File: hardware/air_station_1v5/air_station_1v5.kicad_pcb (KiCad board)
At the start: 2 copper layers, 26.8 x 47.9 mm, 40 parts, among them J1 GCT-SIM7200-XRevA, J2 Micro_SD_Card, J4 BAT_PORT, J5 PROG_PORT, U1 A9G, U3 MCP73831-2-OT, U5 BMP388, U7 AP7312-1833, U9 MIC5225-3.3, X1 ENS160

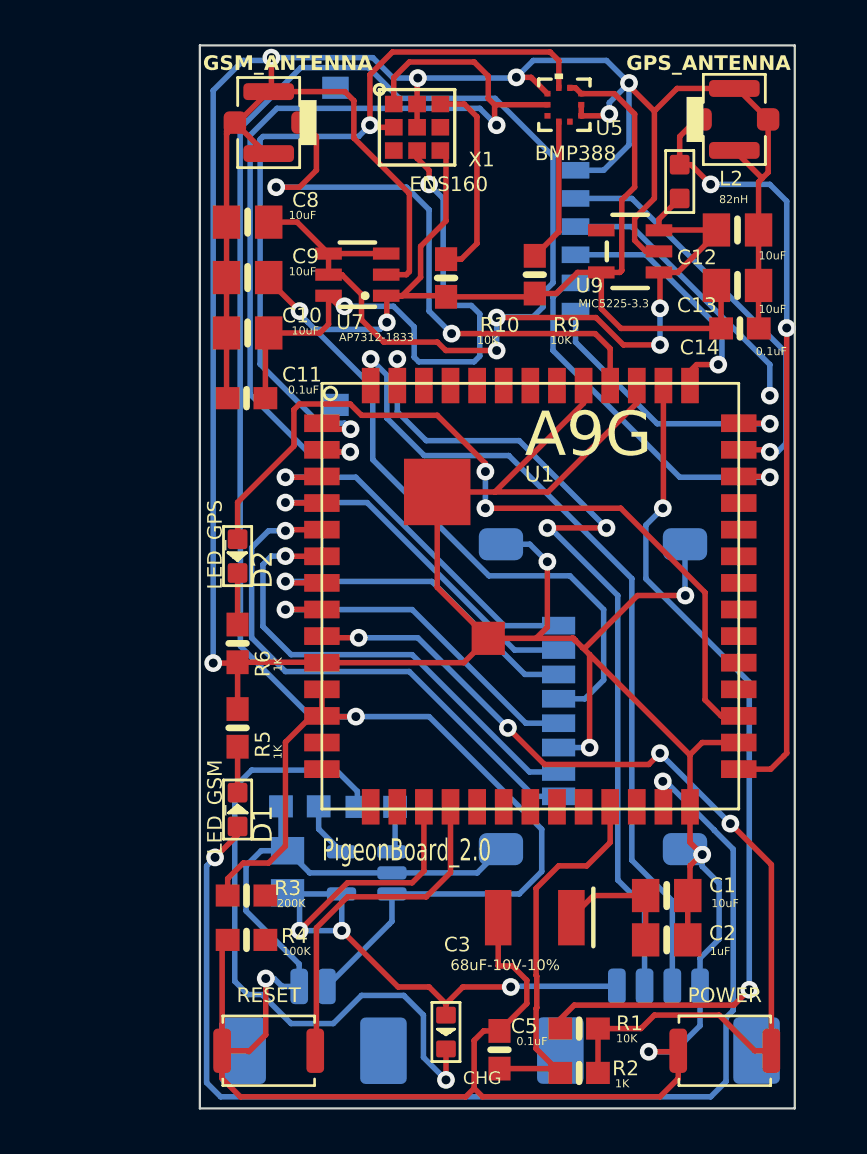
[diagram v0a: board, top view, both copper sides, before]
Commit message: update 1.9
I2C pullups update
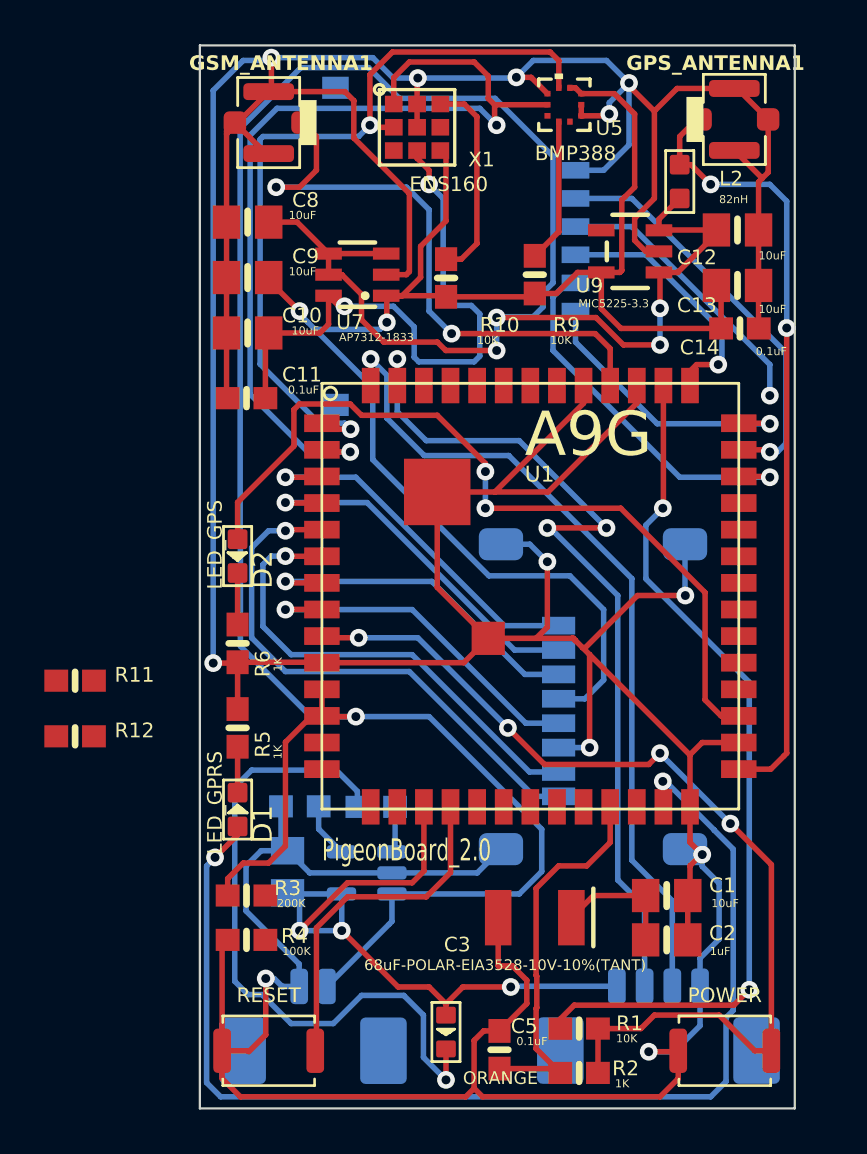
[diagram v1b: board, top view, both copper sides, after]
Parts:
- added R11: 4.7K, Adafruit BMP388:0603-NO, F.Cu at (70.3, 81.3)
- added R12: 4.7K, Adafruit BMP388:0603-NO, F.Cu at (70.3, 83.8)
- C3: value 68uF-10V-10% -> 68uF-POLAR-EIA3528-10V-10%(TANT)
- CHG1: renamed from CHG; value CHG -> ORANGE
- D1: value LED_GSM -> LED_GPRS
- J1: value GCT-SIM7200-XRevA -> SIM7200-6-0-18-00-X_REVA
- renumbered GPS_ANTENNA to GPS_ANTENNA1, GSM_ANTENNA to GSM_ANTENNA1
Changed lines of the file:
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@@
     (property "Sheetfile" "air_station_1v5.kicad_sch")
     (property "Sheetname" "")
-    (fp_text reference "GPS_ANTENNA" (at -4.877 -2.152 180) (layer "F.SilkS")
+    (fp_text reference "GPS_ANTENNA1" (at -4.877 -2.152 180) (layer "F.SilkS")
         (effects (font (size 0.66 0.66) (thickness 0.15) bold) (justify left bottom))
     )
@@
   )
   (footprint "Adafruit BMP388:0603-NO" (layer "F.Cu")
+    (at 70.27 83.82)
+    (property "Sheetfile" "air_station_1v5.kicad_sch")
+    (property "Sheetname" "")
+    (fp_text reference "R12" (at 1.778 0.127) (layer "F.SilkS")
+        (effects (font (size 0.666496 0.666496) (thickness 0.146304)) (justify left bottom))
+    )
+    (fp_text value "4.7K" (at 1.778 0.762) (layer "F.Fab")
+        (effects (font (size 0.36576 0.36576) (thickness 0.04064)) (justify left bottom))
+    )
+    (fp_poly
+      (pts
+        (xy -0.1999 0.3)
+        (xy 0.1999 0.3)
+        (xy 0.1999 -0.3)
+        (xy -0.1999 -0.3)
+      )
+      (stroke (width 0) (type default)) (fill solid) (layer "F.Adhes"))
+    (fp_line (start 0 -0.4) (end 0 0.4)
+      (stroke (width 0.3048) (type solid)) (layer "F.SilkS"))
+    (fp_line (start -1.473 -0.729) (end 1.473 -0.729)
+      (stroke (width 0.0508) (type solid)) (layer "F.CrtYd"))
+    (fp_line (start -1.473 0.729) (end -1.473 -0.729)
+      (stroke (width 0.0508) (type solid)) (layer "F.CrtYd"))
+    (fp_line (start 1.473 -0.729) (end 1.473 0.729)
+      (stroke (width 0.0508) (type solid)) (layer "F.CrtYd"))
+    (fp_line (start 1.473 0.729) (end -1.473 0.729)
+      (stroke (width 0.0508) (type solid)) (layer "F.CrtYd"))
+    (fp_line (start -0.356 -0.432) (end 0.356 -0.432)
+      (stroke (width 0.1016) (type solid)) (layer "F.Fab"))
+    (fp_line (start -0.356 0.419) (end 0.356 0.419)
+      (stroke (width 0.1016) (type solid)) (layer "F.Fab"))
+    (fp_poly
+      (pts
+        (xy -0.8382 0.4699)
+        (xy -0.3381 0.4699)
+        (xy -0.3381 -0.4801)
+        (xy -0.8382 -0.4801)
+      )
+      (stroke (width 0) (type default)) (fill solid) (layer "F.Fab"))
+    (fp_poly
+      (pts
+        (xy 0.3302 0.4699)
+        (xy 0.8303 0.4699)
+        (xy 0.8303 -0.4801)
+        (xy 0.3302 -0.4801)
+      )
+      (stroke (width 0) (type default)) (fill solid) (layer "F.Fab"))
+    (pad "1" smd rect (at -0.85 0) (size 1.075 1) (layers "F.Cu" "F.Paste" "F.Mask")
+      (net 21 "/I2C2_SCL") (pinfunction "1") (pintype "passive") (solder_mask_margin 0.0508) (thermal_bridge_angle 45))
+    (pad "2" smd rect (at 0.85 0) (size 1.075 1) (layers "F.Cu" "F.Paste" "F.Mask")
+      (net 7 "3.3V") (pinfunction "2") (pintype "passive") (solder_mask_margin 0.0508) (thermal_bridge_angle 45))
+  )
+  (footprint "Adafruit BMP388:0603-NO" (layer "F.Cu")
     (at 93 97 180)
     (property "Sheetfile" "air_station_1v5.kicad_sch")
@@
         (effects (font (size 0.66 0.66) (thickness 0.12192)) (justify bottom))
     )
-    (fp_text value "68uF-10V-10%" (at -1.338 1.853) (layer "F.SilkS")
+    (fp_text value "68uF-POLAR-EIA3528-10V-10%(TANT)" (at -1.338 1.853) (layer "F.SilkS")
         (effects (font (size 0.48768 0.48768) (thickness 0.12192)) (justify top))
     )
@@
     (property "Sheetfile" "air_station_1v5.kicad_sch")
     (property "Sheetname" "")
-    (fp_text reference "GSM_ANTENNA" (at -4.693 2.293642 180) (layer "F.SilkS")
+    (fp_text reference "GSM_ANTENNA1" (at -4.693 2.293642 180) (layer "F.SilkS")
         (effects (font (size 0.66 0.66) (thickness 0.15) bold) (justify right bottom))
     )
@@
     )
   )
+  (footprint "Adafruit BMP388:0603-NO" (layer "F.Cu")
+    (at 70.27 81.3112)
+    (property "Sheetfile" "air_station_1v5.kicad_sch")
+    (property "Sheetname" "")
+    (fp_text reference "R11" (at 1.778 0.127) (layer "F.SilkS")
+        (effects (font (size 0.666496 0.666496) (thickness 0.146304)) (justify left bottom))
+    )
+    (fp_text value "4.7K" (at 1.778 0.762) (layer "F.Fab")
+        (effects (font (size 0.36576 0.36576) (thickness 0.04064)) (justify left bottom))
+    )
+    (fp_poly
+      (pts
+        (xy -0.1999 0.3)
+        (xy 0.1999 0.3)
+        (xy 0.1999 -0.3)
+        (xy -0.1999 -0.3)
+      )
+      (stroke (width 0) (type default)) (fill solid) (layer "F.Adhes"))
+    (fp_line (start 0 -0.4) (end 0 0.4)
+      (stroke (width 0.3048) (type solid)) (layer "F.SilkS"))
+    (fp_line (start -1.473 -0.729) (end 1.473 -0.729)
+      (stroke (width 0.0508) (type solid)) (layer "F.CrtYd"))
+    (fp_line (start -1.473 0.729) (end -1.473 -0.729)
+      (stroke (width 0.0508) (type solid)) (layer "F.CrtYd"))
+    (fp_line (start 1.473 -0.729) (end 1.473 0.729)
+      (stroke (width 0.0508) (type solid)) (layer "F.CrtYd"))
+    (fp_line (start 1.473 0.729) (end -1.473 0.729)
+      (stroke (width 0.0508) (type solid)) (layer "F.CrtYd"))
+    (fp_line (start -0.356 -0.432) (end 0.356 -0.432)
+      (stroke (width 0.1016) (type solid)) (layer "F.Fab"))
+    (fp_line (start -0.356 0.419) (end 0.356 0.419)
+      (stroke (width 0.1016) (type solid)) (layer "F.Fab"))
+    (fp_poly
+      (pts
+        (xy -0.8382 0.4699)
+        (xy -0.3381 0.4699)
+        (xy -0.3381 -0.4801)
+        (xy -0.8382 -0.4801)
+      )
+      (stroke (width 0) (type default)) (fill solid) (layer "F.Fab"))
+    (fp_poly
+      (pts
+        (xy 0.3302 0.4699)
+        (xy 0.8303 0.4699)
+        (xy 0.8303 -0.4801)
+        (xy 0.3302 -0.4801)
+      )
+      (stroke (width 0) (type default)) (fill solid) (layer "F.Fab"))
+    (pad "1" smd rect (at -0.85 0) (size 1.075 1) (layers "F.Cu" "F.Paste" "F.Mask")
+      (net 20 "/I2C2_SDA") (pinfunction "1") (pintype "passive") (solder_mask_margin 0.0508) (thermal_bridge_angle 45))
+    (pad "2" smd rect (at 0.85 0) (size 1.075 1) (layers "F.Cu" "F.Paste" "F.Mask")
+      (net 7 "3.3V") (pinfunction "2") (pintype "passive") (solder_mask_margin 0.0508) (thermal_bridge_angle 45))
+  )
   (footprint "Maduino Zero A9G GPS Tracker v3.3:LED-0603" (layer "F.Cu")
     (at 77.597 87.122 90)
@@
         (effects (font (size 0.89408 0.89408) (thickness 0.12192)) (justify left bottom))
     )
-    (fp_text value "LED_GSM" (at -2.032 -0.635 90) (layer "F.SilkS")
+    (fp_text value "LED_GPRS" (at -2.032 -0.635 90) (layer "F.SilkS")
         (effects (font (size 0.66 0.66) (thickness 0.12192)) (justify left bottom))
     )
@@
     (property "Sheetfile" "air_station_1v5.kicad_sch")
     (property "Sheetname" "")
-    (fp_text reference "CHG" (at 2.54 -1.651) (layer "F.Fab")
+    (fp_text reference "CHG1" (at 2.54 -1.651) (layer "F.Fab")
         (effects (font (size 0.5715 0.5715) (thickness 0.0635)) (justify left bottom))
     )
-    (fp_text value "CHG" (at 2.413 -0.762) (layer "F.SilkS")
+    (fp_text value "ORANGE" (at 2.413 -0.762) (layer "F.SilkS")
         (effects (font (size 0.5715 0.5715) (thickness 0.0635)) (justify left bottom))
     )
@@
         (effects (font (size 0.66 0.66) (thickness 0.15)) (justify mirror))
     )
-    (fp_text value "GCT-SIM7200-XRevA" (at 4.444 -0.384) (layer "B.Fab")
+    (fp_text value "SIM7200-6-0-18-00-X_REVA" (at 4.444 -0.384) (layer "B.Fab")
         (effects (font (size 0.66 0.66) (thickness 0.15)) (justify mirror))
     )
@@
     (fp_line (start 7.35 4.1) (end 7.35 6.825)
       (stroke (width 0.2) (type solid)) (layer "B.SilkS"))
-    (fp_arc (start -4.42 -8.175) (mid -2143.062522 -2139.307535) (end -4.42282 -8.17665)
+    (fp_arc (start -4.42 -8.175) (mid -1518.485687 -1518.485687) (end -4.42282 -8.17665)
       (stroke (width 0.1) (type solid)) (layer "Dwgs.User"))
-    (fp_arc (start 4.42282 -8.17665) (mid 2143.061954 -2139.308111) (end 4.42 -8.175)
+    (fp_arc (start 4.42282 -8.17665) (mid 1518.485687 -1518.485687) (end 4.42 -8.175)
       (stroke (width 0.1) (type solid)) (layer "Dwgs.User"))
     (fp_line (start -8 -8.75) (end -8 8.5)
